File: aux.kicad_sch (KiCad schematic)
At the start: 27 parts, among them J7 USB_C_Receptacle_USB2.0_16P, J85 Conn_01x02_Pin, J86 Conn_01x02_Pin, Q81 Si2301CDS, Q82 AO3400A, U85 DAC80508xRTE

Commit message: More component metadata.
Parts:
- C811, C812, C813, C814, C815: value 10u -> 1u; LCSC (none) -> C52923; Stock (none) -> JLC
- C851, C852, C853, C854, D85, L83, L86, Q81, Q82, R86, R87, R88, R89, U85: Stock (none) -> JLC
- J7: Stock (none) -> Bag
- J85, J86: Stock (none) -> Heaps
- R811, R812, R813, R814, R815: LCSC (none) -> C22936; Stock (none) -> JLC
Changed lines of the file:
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@@
 			)
 		)
-		(property "Stock" ""
+		(property "Stock" "JLC"
 			(at 129.54 29.21 90)
 			(effects
@@
 			)
 		)
-		(property "Stock" ""
+		(property "Stock" "JLC"
 			(at 139.7 68.58 0)
 			(effects
@@
 			)
 		)
-		(property "Value" "10u"
+		(property "Value" "1u"
 			(at 102.87 84.328 0)
 			(effects
@@
 			)
 		)
-		(property "Datasheet" "0V"
+		(property "Datasheet" "25V"
 			(at 102.87 86.36 0)
 			(effects
@@
 			)
 		)
-		(property "LCSC" ""
+		(property "LCSC" "C52923"
 			(at 102.87 86.36 0)
 			(effects
@@
 			)
 		)
-		(property "Stock" ""
+		(property "Stock" "JLC"
 			(at 102.87 86.36 0)
 			(effects
@@
 			)
 		)
-		(property "Stock" ""
+		(property "Stock" "JLC"
 			(at 100.33 31.75 90)
 			(effects
@@
 			)
 		)
-		(property "Stock" ""
+		(property "Stock" "JLC"
 			(at 144.78 73.66 0)
 			(effects
@@
 			)
 		)
-		(property "Value" "10u"
+		(property "Value" "1u"
 			(at 96.52 84.328 0)
 			(effects
@@
 			)
 		)
-		(property "Datasheet" "0V"
+		(property "Datasheet" "25V"
 			(at 96.52 86.36 0)
 			(effects
@@
 			)
 		)
-		(property "LCSC" ""
+		(property "LCSC" "C52923"
 			(at 96.52 86.36 0)
 			(effects
@@
 			)
 		)
-		(property "Stock" ""
+		(property "Stock" "JLC"
 			(at 96.52 86.36 0)
 			(effects
@@
 			)
 		)
-		(property "Stock" ""
+		(property "Stock" "JLC"
 			(at 124.46 33.02 90)
 			(effects
@@
 			)
 		)
-		(property "Stock" ""
+		(property "Stock" "JLC"
 			(at 100.33 34.29 90)
 			(effects
@@
 			)
 		)
-		(property "Stock" ""
+		(property "Stock" "Heaps"
 			(at 170.18 29.21 0)
 			(effects
@@
 			)
 		)
-		(property "Value" "10u"
+		(property "Value" "1u"
 			(at 83.82 84.328 0)
 			(effects
@@
 			)
 		)
-		(property "Datasheet" "0V"
+		(property "Datasheet" "25V"
 			(at 83.82 86.36 0)
 			(effects
@@
 			)
 		)
-		(property "LCSC" ""
+		(property "LCSC" "C52923"
 			(at 83.82 86.36 0)
 			(effects
@@
 			)
 		)
-		(property "Stock" ""
+		(property "Stock" "JLC"
 			(at 83.82 86.36 0)
 			(effects
@@
 			)
 		)
-		(property "Stock" ""
+		(property "Stock" "JLC"
 			(at 114.3 31.75 90)
 			(effects
@@
 			)
 		)
-		(property "LCSC" ""
+		(property "LCSC" "C22936"
 			(at 96.52 77.47 90)
 			(effects
@@
 			)
 		)
-		(property "Stock" ""
+		(property "Stock" "JLC"
 			(at 96.52 77.47 90)
 			(effects
@@
 			)
 		)
-		(property "Value" "10u"
+		(property "Value" "1u"
 			(at 77.47 84.328 0)
 			(effects
@@
 			)
 		)
-		(property "Datasheet" "0V"
+		(property "Datasheet" "25V"
 			(at 77.47 86.36 0)
 			(effects
@@
 			)
 		)
-		(property "LCSC" ""
+		(property "LCSC" "C52923"
 			(at 77.47 86.36 0)
 			(effects
@@
 			)
 		)
-		(property "Stock" ""
+		(property "Stock" "JLC"
 			(at 77.47 86.36 0)
 			(effects
@@
 			)
 		)
-		(property "LCSC" ""
+		(property "LCSC" "C22936"
 			(at 77.47 77.47 90)
 			(effects
@@
 			)
 		)
-		(property "Stock" ""
+		(property "Stock" "JLC"
 			(at 77.47 77.47 90)
 			(effects
@@
 			)
 		)
-		(property "LCSC" ""
+		(property "LCSC" "C22936"
 			(at 102.87 77.47 90)
 			(effects
@@
 			)
 		)
-		(property "Stock" ""
+		(property "Stock" "JLC"
 			(at 102.87 77.47 90)
 			(effects
@@
 			)
 		)
-		(property "LCSC" ""
+		(property "LCSC" "C22936"
 			(at 90.17 77.47 90)
 			(effects
@@
 			)
 		)
-		(property "Stock" ""
+		(property "Stock" "JLC"
 			(at 90.17 77.47 90)
 			(effects
@@
 			)
 		)
-		(property "Stock" ""
+		(property "Stock" "JLC"
 			(at 168.91 76.2 0)
 			(effects
@@
 			)
 		)
-		(property "Stock" ""
+		(property "Stock" "Heaps"
 			(at 170.18 39.37 0)
 			(effects
@@
 			)
 		)
-		(property "Stock" ""
+		(property "Stock" "Bag"
 			(at 81.28 41.91 0)
 			(effects
@@
 			)
 		)
-		(property "Stock" ""
+		(property "Stock" "JLC"
 			(at 128.27 64.77 90)
 			(effects
@@
 			)
 		)
-		(property "Stock" ""
+		(property "Stock" "JLC"
 			(at 132.08 40.64 0)
 			(effects
@@
 			)
 		)
-		(property "Stock" ""
+		(property "Stock" "JLC"
 			(at 134.62 68.58 0)
 			(effects
@@
 			)
 		)
-		(property "Stock" ""
+		(property "Stock" "JLC"
 			(at 139.7 30.48 0)
 			(effects
@@
 			)
 		)
-		(property "LCSC" ""
+		(property "LCSC" "C22936"
 			(at 83.82 77.47 90)
 			(effects
@@
 			)
 		)
-		(property "Stock" ""
+		(property "Stock" "JLC"
 			(at 83.82 77.47 90)
 			(effects
@@
 			)
 		)
-		(property "Stock" ""
+		(property "Stock" "JLC"
 			(at 135.89 44.45 90)
 			(effects
@@
 			)
 		)
-		(property "Stock" ""
+		(property "Stock" "JLC"
 			(at 106.68 26.67 90)
 			(effects
@@
 			)
 		)
-		(property "Value" "10u"
+		(property "Value" "1u"
 			(at 90.17 84.328 0)
 			(effects
@@
 			)
 		)
-		(property "Datasheet" "0V"
+		(property "Datasheet" "25V"
 			(at 90.17 86.36 0)
 			(effects
@@
 			)
 		)
-		(property "LCSC" ""
+		(property "LCSC" "C52923"
 			(at 90.17 86.36 0)
 			(effects
@@
 			)
 		)
-		(property "Stock" ""
+		(property "Stock" "JLC"
 			(at 90.17 86.36 0)
 			(effects

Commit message: Contact pads.  Shuffle the big cap.
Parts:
- added J801, J802, J803, J804, J805, J806: Conn_01x01_Pin, Parts:RF_Finger_Side, symbol Connector:Conn_01x01_Pin
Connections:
- net GNDPWR: now also J801.1 (Pin_1), J802.1 (Pin_1), J803.1 (Pin_1), J804.1 (Pin_1), J805.1 (Pin_1), J806.1 (Pin_1)
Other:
- moved on the sheet: J85, J86

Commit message: Tweaks and simplification.
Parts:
- Q81: value Si2301CDS -> AO3401A; symbol Parts:Si2301CDS -> Parts:AO3401A; LCSC C10487 -> C15127
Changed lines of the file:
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@@
-		)
-	)
-	(text_box "Snubbers hopefully damp resonance between reference ground and power ground planes."
-		(exclude_from_sim no)
-		(at 106.68 80.01 0)
-		(size 20.32 11.43)
-		(margins 0.254 0.254 0.254 0.254)
-		(stroke
-			(width 0)
-			(type solid)
-		)
-		(fill
-			(type none)
-		)
-		(effects
-			(font
-				(size 1.27 1.27)
-			)
-			(justify left)
 		)
 	)
@@
 	)
 	(symbol
-		(lib_id "Parts:Si2301CDS")
+		(lib_id "Parts:AO3401A")
 		(at 129.54 29.21 270)
 		(mirror x)
@@
 			)
 		)
-		(property "Value" "Si2301CDS"
+		(property "Value" "AO3401A"
 			(at 129.54 23.368 90)
 			(effects
@@
 		)
 		(property "Footprint" "Parts:SOT-23"
-			(at 127.635 24.13 0)
-			(effects
-				(font
-					(size 1.27 1.27)
-					(italic yes)
-				)
-				(justify left)
+			(at 132.08 24.13 0)
+			(effects
+				(font
+					(size 1.27 1.27)
+				)
 				(hide yes)
 			)
 		)
 		(property "Datasheet" "~"
-			(at 125.73 24.13 0)
-			(effects
-				(font
-					(size 1.27 1.27)
-				)
-				(justify left)
+			(at 129.54 29.21 0)
+			(effects
+				(font
+					(size 1.27 1.27)
+				)
 				(hide yes)
 			)
@@
 			)
 		)
-		(property "LCSC" "C10487"
-			(at 129.54 29.21 90)
-			(effects
-				(font
+		(property "LCSC" "C15127"
+			(at 129.54 29.21 0)
+			(effects
+				(font

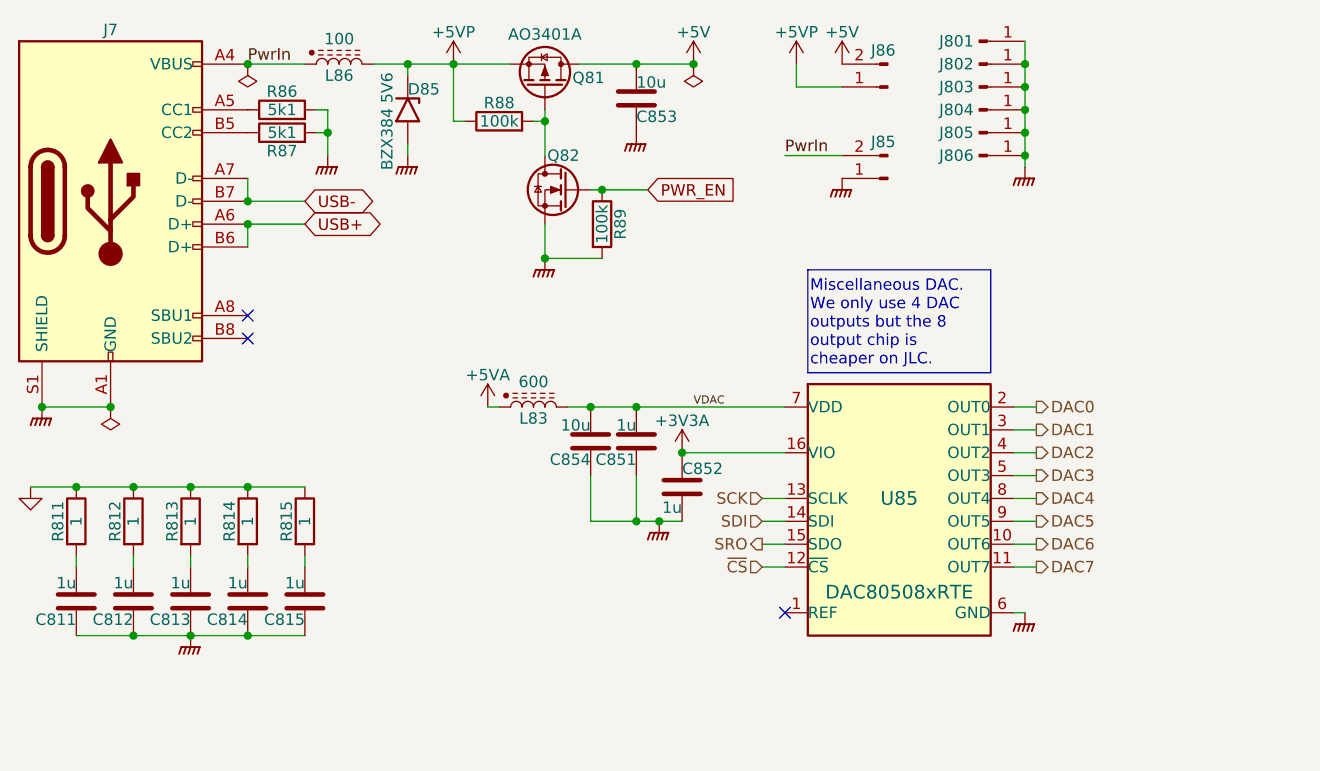
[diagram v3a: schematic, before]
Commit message: Add some bulk capacitance.
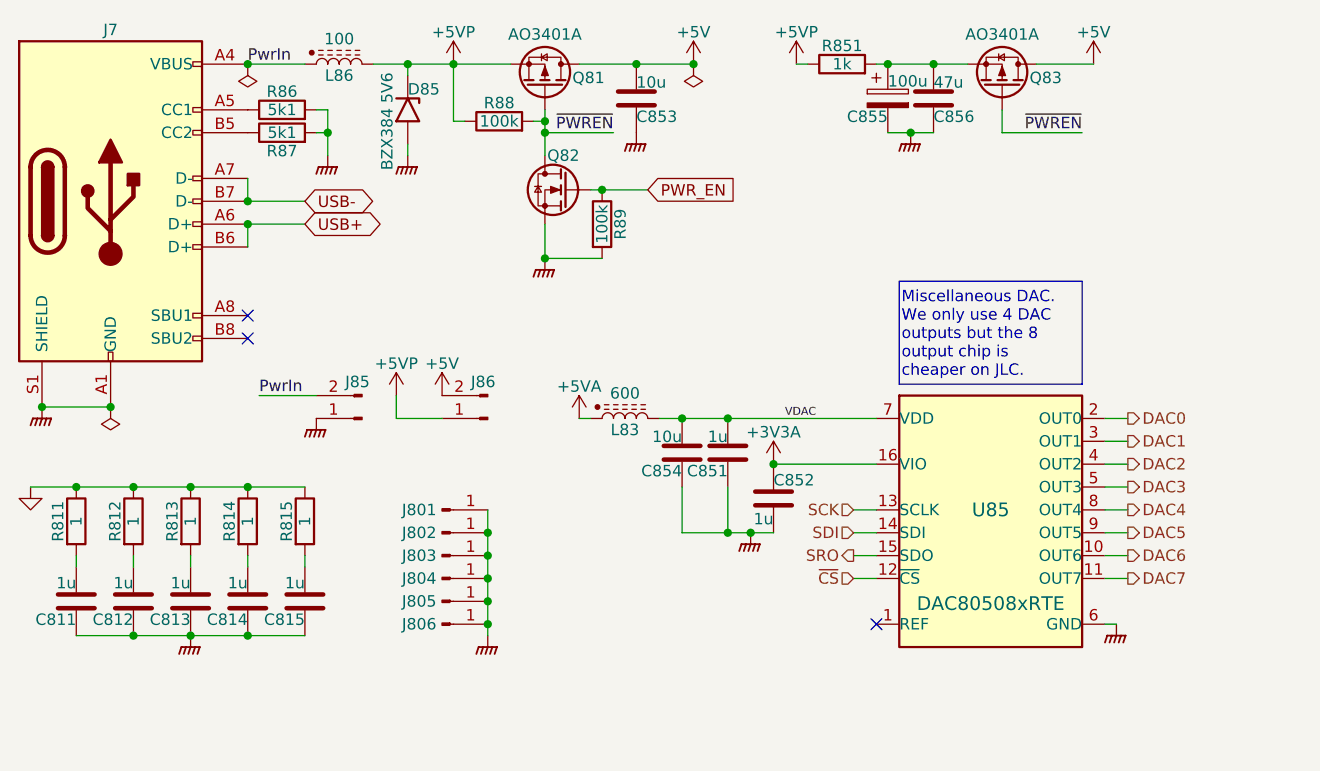
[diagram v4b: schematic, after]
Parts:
- added C855: 100u, Capacitor_Tantalum_SMD:CP_EIA-3528-12_Kemet-T, symbol Device:C_Polarized
- added C856: 47u, Capacitor_SMD:C_1206_3216Metric, symbol Device:C
- added Q83: AO3401A, Parts:SOT-23, symbol Parts:AO3401A
- added R851: 1k, Resistor_SMD:R_0402_1005Metric, symbol Device:R
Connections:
- net +5V: now also Q83.3 (D)
- net +5VP: now also R851.1
- net GNDPWR: now also C855.2, C856.2
- net ~{PWREN}: now reaches Q81.1 (G), Q82.3 (D), R88.2
- net ~{PWREN}: now also Q83.1 (G)
- new net: C855.1, C856.1, Q83.2 (S), R851.2
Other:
- moved on the sheet: C851, C852, C854, J801, J802, J803, J804, J805, J806, J85, J86, L83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

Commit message: Component tweak.
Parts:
- R851: value 1k -> 100; footprint Resistor_SMD:R_0402_1005Metric -> Resistor_SMD:R_0603_1608Metric; LCSC C11702 -> C22775
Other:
- moved on the sheet: J85, J86
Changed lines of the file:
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@@
 	(generator_version "9.0")
 	(paper "A4")
-	(text_box "Miscellaneous DAC.\nWe only use 4 DAC outputs but the 8 output chip is cheaper on JLC."
+	(text_box "Miscellaneous DAC. We only use 4 DAC outputs but the 8 output chip is cheaper on JLC."
 		(exclude_from_sim no)
 		(at 168.91 50.8 0)
@@
 	(wire
 		(pts
-			(xy 113.03 66.04) (xy 118.11 66.04)
+			(xy 170.18 45.72) (xy 175.26 45.72)
 		)
 		(stroke
@@
 	(wire
 		(pts
-			(xy 113.03 63.5) (xy 113.03 66.04)
+			(xy 170.18 43.18) (xy 170.18 45.72)
 		)
 		(stroke
@@
 	(wire
 		(pts
-			(xy 97.79 63.5) (xy 104.14 63.5)
+			(xy 106.68 59.69) (xy 113.03 59.69)
 		)
 		(stroke
@@
 	)
 	(label "PwrIn"
-		(at 97.79 63.5 0)
+		(at 106.68 59.69 0)
 		(effects
 			(font
@@
 	(symbol
 		(lib_id "Connector:Conn_01x02_Pin")
-		(at 123.19 66.04 180)
+		(at 180.34 45.72 180)
 		(unit 1)
 		(exclude_from_sim no)
@@
 		(dnp no)
 		(property "Reference" "J86"
-			(at 122.682 61.976 0)
+			(at 179.832 41.656 0)
 			(effects
 				(font
@@
 		)
 		(property "Value" "Conn_01x02_Pin"
-			(at 123.19 60.96 0)
+			(at 180.34 40.64 0)
 			(effects
 				(font
@@
 		)
 		(property "Footprint" "Parts:PinHeader_1x02_P2.54mm_Vertical"
-			(at 123.19 66.04 0)
+			(at 180.34 45.72 0)
 			(effects
 				(font
@@
 		)
 		(property "Datasheet" "~"
-			(at 123.19 66.04 0)
+			(at 180.34 45.72 0)
 			(effects
 				(font
@@
 		)
 		(property "Description" "Generic connector, single row, 01x02, script generated"
-			(at 123.19 66.04 0)
+			(at 180.34 45.72 0)
 			(effects
 				(font
@@
 		)
 		(property "Stock" "Heaps"
-			(at 123.19 66.04 0)
+			(at 180.34 45.72 0)
 			(effects
 				(font
@@
 	(symbol
 		(lib_id "power:+5VP")
-		(at 113.03 63.5 0)
+		(at 170.18 43.18 0)
 		(unit 1)
 		(exclude_from_sim no)
@@
 		(dnp no)
 		(property "Reference" "#PWR0161"
-			(at 113.03 67.31 0)
+			(at 170.18 46.99 0)
 			(effects
 				(font
@@
 		)
 		(property "Value" "+5VP"
-			(at 113.03 59.944 0)
+			(at 170.18 39.624 0)
 			(effects
 				(font
@@
 		)
 		(property "Footprint" ""
-			(at 113.03 63.5 0)
+			(at 170.18 43.18 0)
 			(effects
 				(font
@@
 		)
 		(property "Datasheet" ""
-			(at 113.03 63.5 0)
+			(at 170.18 43.18 0)
 			(effects
 				(font
@@
 		)
 		(property "Description" "Power symbol creates a global label with name \"+5VP\""
-			(at 113.03 63.5 0)
+			(at 170.18 43.18 0)
 			(effects
 				(font
@@
 			)
 		)
-		(property "Value" "1k"
+		(property "Value" "100"
 			(at 162.56 26.67 90)
 			(effects
@@
 			)
 		)
-		(property "Footprint" "Resistor_SMD:R_0402_1005Metric"
+		(property "Footprint" "Resistor_SMD:R_0603_1608Metric"
 			(at 162.56 28.448 90)
 			(effects
@@
 			)
 		)
-		(property "LCSC" "C11702"
+		(property "LCSC" "C22775"
 			(at 162.56 26.67 90)
 			(effects
@@
 	(symbol
 		(lib_id "power:+5V")
-		(at 118.11 63.5 0)
+		(at 175.26 43.18 0)
 		(unit 1)
 		(exclude_from_sim no)
@@
 		(dnp no)
 		(property "Reference" "#PWR0160"
-			(at 118.11 67.31 0)
+			(at 175.26 46.99 0)
 			(effects
 				(font
@@
 		)
 		(property "Value" "+5V"
-			(at 118.11 59.944 0)
+			(at 175.26 39.624 0)
 			(effects
 				(font
@@
 		)
 		(property "Footprint" ""
-			(at 118.11 63.5 0)
+			(at 175.26 43.18 0)
 			(effects
 				(font
@@
 		)
 		(property "Datasheet" ""
-			(at 118.11 63.5 0)
+			(at 175.26 43.18 0)
 			(effects
 				(font
@@
 		)
 		(property "Description" "Power symbol creates a global label with name \"+5V\""
-			(at 118.11 63.5 0)
+			(at 175.26 43.18 0)
 			(effects
 				(font
@@
 	(symbol
 		(lib_id "Connector:Conn_01x02_Pin")
-		(at 109.22 66.04 180)
+		(at 118.11 62.23 180)
 		(unit 1)
 		(exclude_from_sim no)
@@
 		(dnp no)
 		(property "Reference" "J85"
-			(at 108.712 61.976 0)
+			(at 117.602 58.166 0)
 			(effects
 				(font
@@
 		)
 		(property "Value" "Conn_01x02_Pin"
-			(at 109.22 60.96 0)
+			(at 118.11 57.15 0)
 			(effects
 				(font
@@
 		)
 		(property "Footprint" "Parts:PinHeader_1x02_P2.54mm_Vertical"
-			(at 109.22 66.04 0)
+			(at 118.11 62.23 0)
 			(effects
 				(font
@@
 		)
 		(property "Datasheet" "~"
-			(at 109.22 66.04 0)
+			(at 118.11 62.23 0)
 			(effects
 				(font
@@
 		)
 		(property "Description" "Generic connector, single row, 01x02, script generated"
-			(at 109.22 66.04 0)
+			(at 118.11 62.23 0)
 			(effects
 				(font
@@
 		)
 		(property "Stock" "Heaps"
-			(at 109.22 66.04 0)
+			(at 118.11 62.23 0)
 			(effects
 				(font
@@
 	(symbol
 		(lib_id "power:GNDPWR")
-		(at 104.14 66.04 0)
+		(at 113.03 62.23 0)
 		(unit 1)
 		(exclude_from_sim no)
@@
 		(dnp no)
 		(property "Reference" "#PWR0162"
-			(at 104.14 72.39 0)
+			(at 113.03 68.58 0)
 			(effects
 				(font
@@
 		)
 		(property "Value" "GNDPWR"
-			(at 104.14 69.342 0)
+			(at 113.03 65.532 0)
 			(effects
 				(font
@@
 		)
 		(property "Footprint" ""
-			(at 104.14 67.31 0)
+			(at 113.03 63.5 0)
 			(effects
 				(font
@@
 		)
 		(property "Datasheet" ""
-			(at 104.14 67.31 0)
+			(at 113.03 63.5 0)
 			(effects
 				(font
@@
 		)
 		(property "Description" "Power symbol creates a global label with name \"GNDPWR\" , global ground"
-			(at 104.14 66.04 0)
+			(at 113.03 62.23 0)
 			(effects
 				(font

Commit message: Tweak various feedback loops.
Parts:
- C855: Stock (none) -> JLC
- Q82: LCSC C15127 -> C20917
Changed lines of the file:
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@@
+			)
+		)
+		(property "Stock" "JLC"
+			(at 167.64 30.48 0)
+			(effects
+				(font
+					(size 1.27 1.27)
+				)
+				(hide yes)
 			)
 		)
@@
 			)
 		)
-		(property "LCSC" "C15127"
+		(property "LCSC" "C20917"
 			(at 132.08 40.64 0)
 			(effects

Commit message: Readyish
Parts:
- C855: footprint Capacitor_Tantalum_SMD:CP_EIA-3528-12_Kemet-T -> Parts:CP_EIA-3528-12
- J7: footprint Connector_USB:USB_C_Receptacle_GCT_USB4105-xx-A_16P_TopMnt_Horizontal -> Parts:USB_C_Receptacle_GCT_USB4105-xx-A_16P_TopMnt_Horizontal
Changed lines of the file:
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@@
 			)
 		)
-		(property "Footprint" "Capacitor_Tantalum_SMD:CP_EIA-3528-12_Kemet-T"
+		(property "Footprint" "Parts:CP_EIA-3528-12"
 			(at 168.6052 34.29 0)
 			(effects
@@
 			)
 		)
-		(property "Footprint" "Connector_USB:USB_C_Receptacle_GCT_USB4105-xx-A_16P_TopMnt_Horizontal"
+		(property "Footprint" "Parts:USB_C_Receptacle_GCT_USB4105-xx-A_16P_TopMnt_Horizontal"
 			(at 85.09 41.91 0)
 			(effects
